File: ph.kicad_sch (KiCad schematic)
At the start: 17 parts, among them IC2 ADM3260ARSZ-RL7, J25 Conn_01x03_Socket, J26 Conn_01x03_Socket, J4 pH

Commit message: Change pH pinsocket connector from THT to SMD
Closes #42
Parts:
- J25, J26: footprint Connector_PinSocket_2.54mm:PinSocket_1x03_P2.54mm_Vertical -> Connector_PinSocket_2.54mm:PinSocket_1x03_P2.54mm_Vertical_SMD_Pin1Left; LCSC C541850 -> C42379196
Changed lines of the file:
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@@
 			)
 		)
-		(property "Footprint" "Connector_PinSocket_2.54mm:PinSocket_1x03_P2.54mm_Vertical"
+		(property "Footprint" "Connector_PinSocket_2.54mm:PinSocket_1x03_P2.54mm_Vertical_SMD_Pin1Left"
 			(at 165.1 43.18 0)
 			(hide yes)
@@
 			)
 		)
-		(property "LCSC" "C541850"
+		(property "LCSC" "C42379196"
 			(at 165.1 43.18 0)
 			(hide yes)
@@
 			)
 		)
-		(property "Footprint" "Connector_PinSocket_2.54mm:PinSocket_1x03_P2.54mm_Vertical"
+		(property "Footprint" "Connector_PinSocket_2.54mm:PinSocket_1x03_P2.54mm_Vertical_SMD_Pin1Left"
 			(at 152.4 43.18 0)
 			(hide yes)
@@
 			)
 		)
-		(property "LCSC" "C541850"
+		(property "LCSC" "C42379196"
 			(at 152.4 43.18 0)
 			(hide yes)

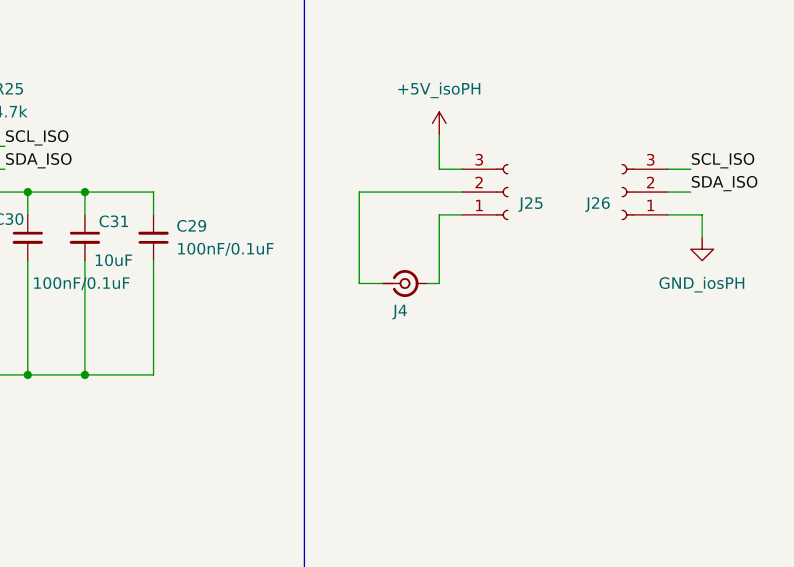
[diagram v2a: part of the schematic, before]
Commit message: Update fabrication properties
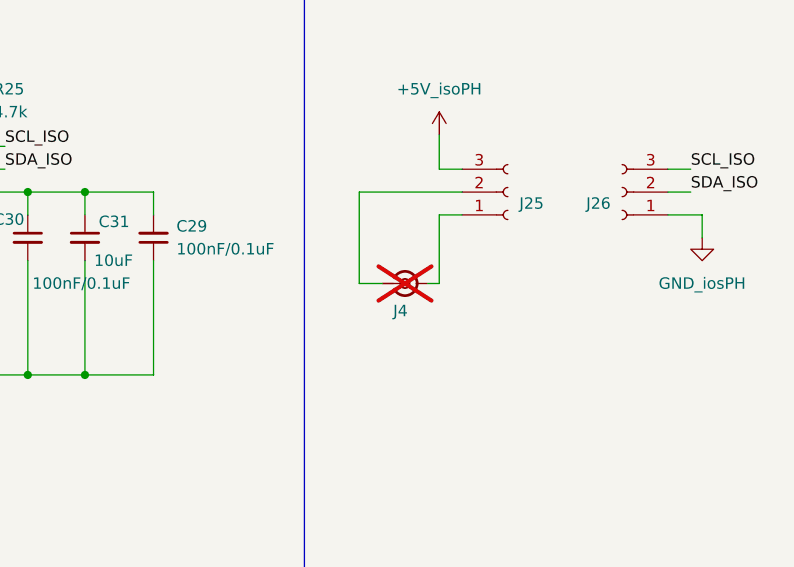
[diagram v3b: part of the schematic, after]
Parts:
- J4: now not fitted; now in the parts list
- R26: LCSC C23022 -> C2930090
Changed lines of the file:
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@@
 		(body_style 1)
 		(exclude_from_sim no)
-		(in_bom no)
+		(in_bom yes)
 		(on_board yes)
 		(in_pos_files yes)
-		(dnp no)
+		(dnp yes)
 		(property "Reference" "J4"
 			(at 140.462 56.388 0)
@@
 			)
 		)
-		(property "LCSC" "C23022"
-			(at 87.63 48.26 0)
-			(hide yes)
-			(show_name no)
-			(do_not_autoplace no)
-			(effects
-				(font
-					(size 1.27 1.27)
-				)
-			)
-		)
-		(property "LCSC alt" ""
+		(property "LCSC" "C2930090"
 			(at 87.63 48.26 0)
 			(hide yes)
@@
 		(in_bom no)
 		(on_board yes)
-		(in_pos_files yes)
+		(in_pos_files no)
 		(dnp no)
 		(property "Reference" "TP6"

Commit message: Update fabrication properties
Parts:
- IC2: FT Rotation Offset (none) -> 270; JLCPCB Rotation Offset 270 -> (none)
- J25, J26: FT Rotation Offset (none) -> 270; JLCPCB Rotation Offset 90 -> (none)
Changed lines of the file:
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@@
 			)
 		)
-		(property "JLCPCB Rotation Offset" "90"
+		(property "FT Rotation Offset" "270"
 			(at 165.1 43.18 0)
 			(hide yes)
@@
 			)
 		)
-		(property "JLCPCB Rotation Offset" "270"
+		(property "FT Rotation Offset" "270"
 			(at 40.64 35.56 0)
 			(hide yes)
@@
 			)
 		)
-		(property "JLCPCB Rotation Offset" "90"
+		(property "FT Rotation Offset" "270"
 			(at 152.4 43.18 0)
 			(hide yes)
